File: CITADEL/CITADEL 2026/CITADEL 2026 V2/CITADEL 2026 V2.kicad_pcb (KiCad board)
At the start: 2 copper layers, 141.5 x 109.7 mm, 72 parts, among them U1 ESP32-S3-DEVKITC-1-N8R8

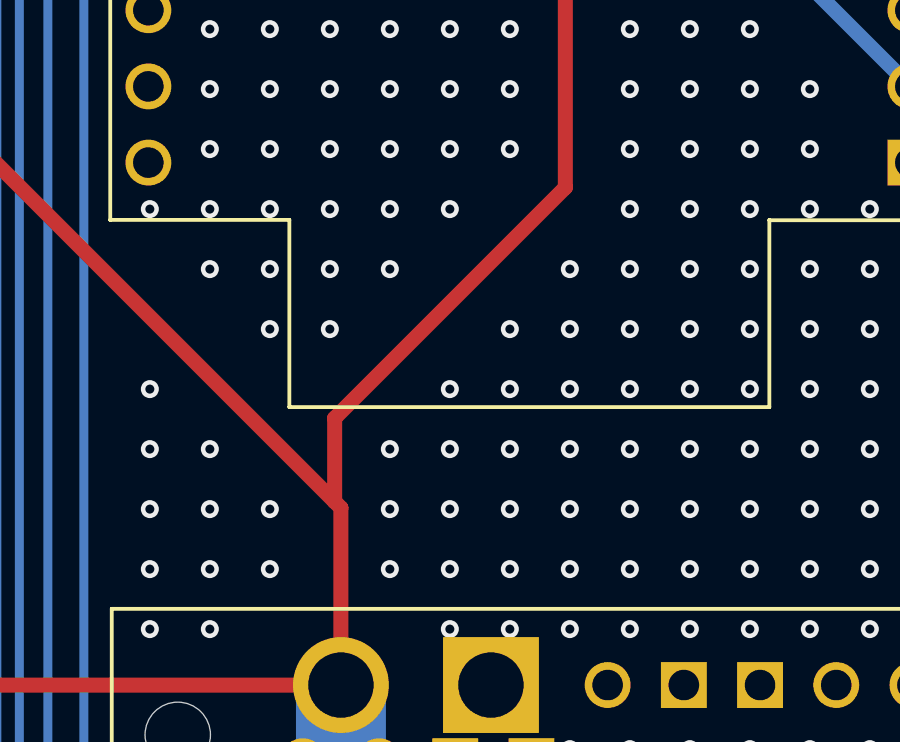
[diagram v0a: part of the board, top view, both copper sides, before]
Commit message: Cleaned up a trace
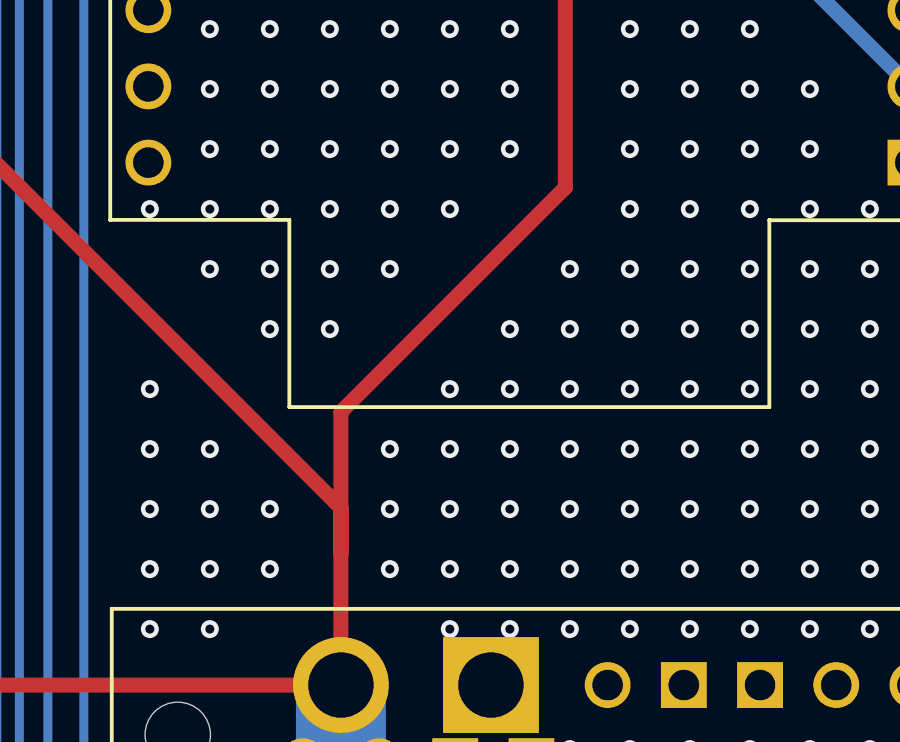
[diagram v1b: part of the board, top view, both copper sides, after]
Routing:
- net +5V: track 454.8 -> 456.4 mm
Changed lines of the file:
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@@
+	)
+	(segment
+		(start 92.85 69.28)
+		(end 92.85 62.26)
+		(width 0.5)
+		(layer "F.Cu")
+		(net 4)
 	)
 	(segment
@@
 	)
 	(segment
-		(start 85.16 76.97)
+		(start 85.37 76.76)
 		(end 92.85 69.28)
 		(width 0.5)
@@
 	)
 	(segment
-		(start 92.85 69.28)
-		(end 92.85 62.26)
+		(start 85.37 81.5)
+		(end 85.37 76.76)
 		(width 0.5)
 		(layer "F.Cu")
@@
 		(width 0.5)
 		(layer "F.Cu")
-		(net 4)
-	)
-	(segment
-		(start 85.16 79.75)
-		(end 85.16 76.97)
-		(width 0.5)
-		(layer "F.Cu")
